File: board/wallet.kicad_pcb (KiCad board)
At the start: 4 copper layers, 48 x 85 mm, 136 parts, among them J1 TYPE-C-31-M-12, U1 BQ25185DLHR, U10 SN74LVC1T45DBVR, U11 E73-2G4M08S1C, U12 ME6211C28M5G-N, U13 TPS60230RGTR, U14 TLV75801PDBVR, U15 MAX17048G+T10, U2 TPS63802DLAR, U3 XC6206P332MR-G, U4 STM32U585VIT6Q, U5 SE050E2HQ1/Z01Z3Z, U6 TS3USB221ARSER, U7 SN74LVC1G02DBVR(UMW), U8 TPS22917DBVR, U9 SN74LVC1T45DBVR, Y1 Q13FC13500049

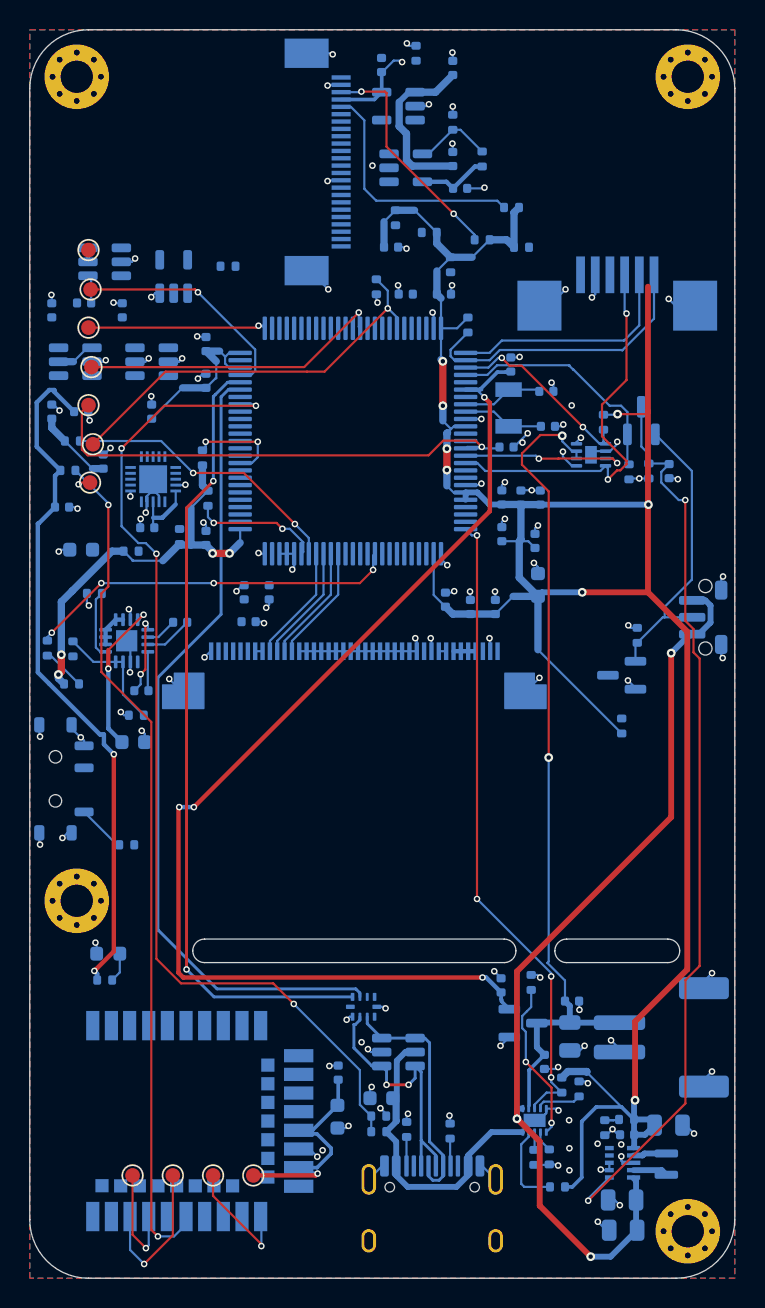
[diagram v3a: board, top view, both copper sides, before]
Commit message: Simplify the netlist (-28 parts), rip my auto-routing, camera pins ordered for J_CAM
Owner review: the pre-route was sloppy and the board too dense. This keeps all
of the owner's copper (minus what sat on removed parts or vanished nets) and
removes every track and via my partial router added.

Removed / merged (research in the commit's PR notes; each change checked
against the part's datasheet):
- radio UART isolation: two SN74LVC1T45 + 4 caps + 3 pull-ups -> one TI
  TXU0202 (fixed A1->B1Y, B2->A2Y; Hi-Z below 100 mV on either supply,
  Ioff; SCES942A 9.3.4) + 2 caps; OE on RADIO_3V3, so the hardware airgap
  guarantee is unchanged
- RTC backup chain (XC6206, 2 caps) and the 32 kHz crystal + 2 caps: VBAT on
  V3V3 (keeps its 100 nF); USB on HSI48+CRS, timeouts on LSI
- VREF+ shares VDDA's caps; VDD11's optional 100 nF caps
- camera: PWDN tied low at J_CAM, no RESET/PWDN pull-ups; DVDD on a fixed
  TLV70313 (no divider); one input cap for both camera LDOs
- R_CTPRST, R_BTNN (PA0 internal pull-up), R_ALRT + GAUGE_ALRT
- test pads SWO, BOOT0, RADIO_RESET
Camera pins: XCLK from TIM3_CH2 on PB5 and RST on PE0, so the north row is
in J_CAM's order (camera-bus trial route: 36 vias vs 40).

Tooling: syncBoard no longer segfaults swapping a back-side land (add before
Flip); checkMcuAf also catches nets dropped from the table; optimizePins can
put a timer clock on any TIMx_CHy pin; partialRoute: back-copper block wiring,
power may use In2, no necking, GND fanout vias keep 0.25 mm from pads, only
caps and ICs get their own GND via, long block links left with their bus.

Co-Authored-By: Claude Opus 5.5 <noreply@anthropic.com>
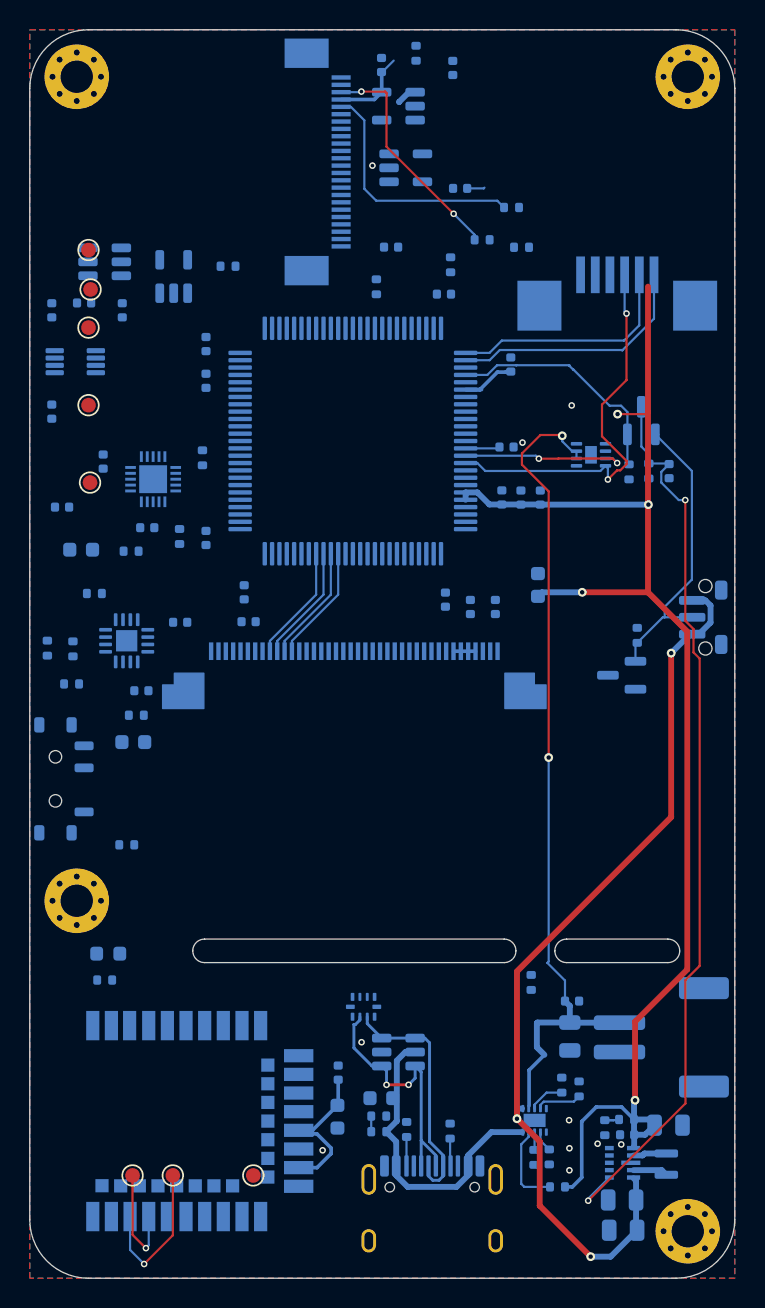
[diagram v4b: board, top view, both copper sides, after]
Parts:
- removed C_DVIN, C_RTC, C_RTCIN, C_VREF1: 1uF, Capacitor_SMD:C_0402_1005Metric
- removed C_LSE1, C_LSE2: 8pF, Capacitor_SMD:C_0402_1005Metric
- removed C_U10A, C_U10B, C_VDD11C, C_VDD11D, C_VREF2: 100nF, Capacitor_SMD:C_0402_1005Metric
- removed R_ALRT, R_BTNN, R_CRST, R_DV2, R_PWDN, R_RMTX, R_RRXPU, R_RTXPU: 100k, Resistor_SMD:R_0402_1005Metric
- removed R_CTPRST: 10k, Resistor_SMD:R_0402_1005Metric
- removed R_DV1: 137k, Resistor_SMD:R_0402_1005Metric
- removed TP_BOOT0: TP_BOOT0, TestPoint:TestPoint_Pad_D1.0mm
- removed TP_RRESET: TP_RRESET, TestPoint:TestPoint_Pad_D1.0mm
- removed TP_SWO: TP_SWO, TestPoint:TestPoint_Pad_D1.0mm
- removed U10: SN74LVC1T45DBVR, Package_TO_SOT_SMD:SOT-23-6
- removed U3: XC6206P332MR-G, Package_TO_SOT_SMD:SOT-23
- removed Y1: Q13FC13500049, Crystal:Crystal_SMD_3215-2Pin_3.2x1.5mm
- U14: value TLV75801PDBVR -> TLV70313DBVR
- U9: value SN74LVC1T45DBVR -> TXU0202DCUR; footprint Package_TO_SOT_SMD:SOT-23-6 -> Package_SO:VSSOP-8_2.3x2mm_P0.5mm
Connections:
- C_VBAT pad 1: VBAT_RTC -> V3V3
- J_CAM pad 17: CAM_PWDN -> GND
- U11 pad 26: RADIO_RESET -> (no net)
- U14 pad 4: CAM_DVFB -> GND
- U15 pad 5: GAUGE_ALRT -> NC_GAUGE_ALRT
- U4 pad 3: GAUGE_ALRT -> (no net)
- U4 pad 6: VBAT_RTC -> V3V3
- U4 pad 62: CAM_PWDN -> (no net)
- U4 pad 67: CAM_XCLK -> (no net)
- U4 pad 8: LSE_IN -> (no net)
- U4 pad 88: CAM_RST -> (no net)
- U4 pad 89: SWO -> (no net)
- U4 pad 9: LSE_OUT -> (no net)
- U4 pad 91: (no net) -> CAM_XCLK
- U4 pad 97: (no net) -> CAM_RST
- U9 pad 1: V3V3 -> RADIO_TX
- U9 pad 3: RADIO_TXD_MCU -> V3V3
- U9 pad 4: RADIO_RX -> RADIO_RXD_MCU
- U9 pad 5: V3V3 -> RADIO_TXD_MCU
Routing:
- net V3V3: track 236.9 -> 102.7 mm, vias 12 -> 4
- net GND: track 118.8 -> 1.20 mm, vias 122 -> 10
- net VBAT_RTC: track 78.7 -> 0.00 mm, vias 4 -> 0
- net VBUS_SENSE: track 69.0 -> 1.06 mm, vias 4 -> 0
- net RADIO_TX: track 57.7 -> 0.00 mm, vias 2 -> 0
- net USB_DN_MCU: track 55.4 -> 0.00 mm
- net USB_DP_MCU: track 54.1 -> 0.00 mm, vias 2 -> 0
- net RADIO_3V3: track 64.1 -> 10.1 mm, vias 3 -> 0
- net CHG_STAT2: track 44.0 -> 2.71 mm, vias 4 -> 0
- net NRST: track 34.7 -> 2.34 mm, vias 1 -> 0
- net BOOT0: track 27.8 -> 0.00 mm, vias 1 -> 0
- net AIRGAP_SENSE: track 25.5 -> 0.00 mm, vias 4 -> 0
- net SWO: track 20.9 -> 0.00 mm, vias 1 -> 0
- net RADIO_TXD_MCU: track 19.4 -> 0.00 mm, vias 2 -> 0
- net SWDIO: track 15.5 -> 0.00 mm, vias 1 -> 0
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
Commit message: Placement for routing: camera fan-in cleared, radio translator at the radio, decaps at their pins
- J_CAM's pads are entered from the east, where the camera LDOs left 1.2 mm
  for 24 lines: the LDO cluster (now ME6211 + fixed TLV70313, shared input
  cap) moved east of a 3.1 mm "Camera fan-in" keep-out, BOOT0's pull-down out
  of the bus approach. Your camera SDA/SCL/AVDD tracks there are removed.
- J_CAM stays: moved 4.5 mm east (to take a stock 21 mm module flat) its body
  would sit over the MCU's north pin row and cost every north camera pin a via.
  checkFpc now holds the camera tail to a budget: stock modules bow 4.2-4.8 mm
  (a ~16.5 mm custom flex lies flat).
- TXU0202 moved to the strip between the TFT slot and the radio module, right
  over the module's north-edge pads; the radio UART moves to P0.31/P0.30
  (pads 9/10), so no radio line crosses under the module.
- "MCU west escape" keep-out (pins 52-67): the SE pull-up moved out of it.
- Decaps at their pins: VDD11 one per pin (49, 98), C_VBAT clear of the
  PWR_HOLD track that ran between its pads, the battery gauge's cap at the gauge.
- scripts/refreshKeepouts.py redraws the rule areas on a hand-worked board
  from newBoard.py (the camera flex and fan-in follow J_CAM).

DRC: no errors besides 13 starved GND thermals (fanouts come with routing)
and the owner's pre-existing 8.5 mm V3V3 F.Cu stub.

Co-Authored-By: Claude Opus 5.5 <noreply@anthropic.com>
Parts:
- moved U9 44.2 mm to (15.1, 65.1), turned to 0 degrees
- moved C_U9A 40.5 mm to (12.2, 65.1), turned to -90 degrees
- moved C_GAUGE 37.2 mm to (35.9, 28.9), turned to -90 degrees
- moved C_U9B 36.2 mm to (18.0, 65.1), turned to 90 degrees
- moved C_VDD11B 23.7 mm to (27.4, 18.3)
- moved R_CAMEN 7.61 mm to (32.2, 6.40), turned to 0 degrees
- moved R_BOOT0 7.60 mm to (31.2, 17.4), turned to 0 degrees
- moved C_DOVDD 6.21 mm to (28.1, 9.70), turned to 180 degrees
- moved R_CSCL 5.87 mm to (27.4, 14.4), turned to 90 degrees
- moved C_DVOUT 5.74 mm to (26.1, 6.00), turned to 90 degrees
- moved U12 4.07 mm to (28.8, 3.50)
- moved U14 3.94 mm to (28.8, 7.10), turned to 180 degrees
- moved R_SESDA 3.16 mm to (9.00, 27.6), turned to 0 degrees
- moved C_VDD11A 2.95 mm to (16.3, 37.7), turned to -90 degrees
- moved C_AVIN 2.82 mm to (31.6, 2.90), turned to -90 degrees
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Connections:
- U11 pad 10: (no net) -> RADIO_RX
- U11 pad 33: RADIO_TX -> (no net)
- U11 pad 35: RADIO_RX -> (no net)
- U11 pad 9: (no net) -> RADIO_TX
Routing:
- net CAM_SCL: track 16.7 -> 0.00 mm
- net CAM_SDA: track 15.6 -> 0.00 mm, vias 2 -> 0
- net V3V3: track 102.7 -> 97.1 mm
- net CAM_AVDD: track 5.50 -> 0.00 mm
- net GND: track 1.20 -> 0.00 mm, vias 10 -> 9

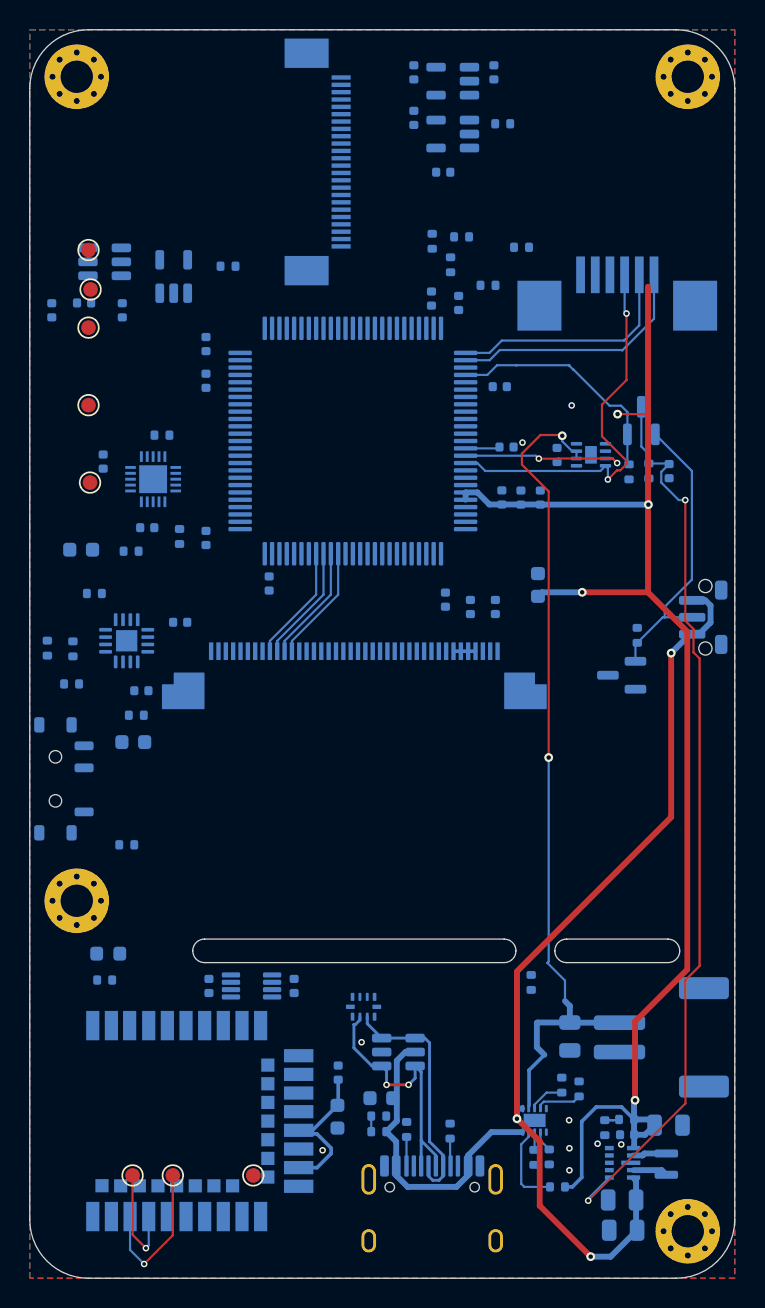
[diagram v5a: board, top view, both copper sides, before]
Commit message: Stack-up fixed (In2 solid GND, In1 the 3.3 V plane); blocks pre-routed cleanly
Stack-up: every part sits on B.Cu, whose return currents run in In2, but In2
was the "GND poured around power runs" layer and In1 the solid GND. Swapped:
In2 is solid GND (DRU: GND only), In1 is a V3V3 plane (DRU: V3V3, plus the
VDD11 core link). Every V3V3 pin and decap now drops a short via to In1, so no
3.3 V trunk runs on the outer layers.

Block wiring (scripts/partialRoute.py, on humanRouter's new keep-copper API
and knobs): back copper only; GND vias only for caps and ICs, 0.25 mm clear
of every pad, plus any pad the pour starves; no necking; test-pad, pull-up
and power links longer than 7/10 mm are left with their highway. Result: 144/145
block links + plane fanouts; new copper 202 mm B.Cu, 16 mm In1 (VDD11),
5 mm F.Cu (one radio test pad); the front is free for the highways.

Placement for this: the backlight pump turned 180 deg (cathodes/VOUT toward
J_TFT, flying caps west, input/output caps at VIN/VOUT, which the loop around
the chip showed); the SE 1.1 mm west with its input cap at VIN and its pull-ups
at their pins; BOOT0 tied to GND (bootloader via option bytes) so no pull-down
link crosses the camera pins, its via inside the pin ring.

Gauges on what is left for the hand route: KiCadRoutingTools routes all of it
(0 failed, 119 vias; before this pass 2-5 nets failed); humanRouter's full
finish routes all of it too (0 unconnected, 230 s).

Co-Authored-By: Claude Opus 5.5 <noreply@anthropic.com>
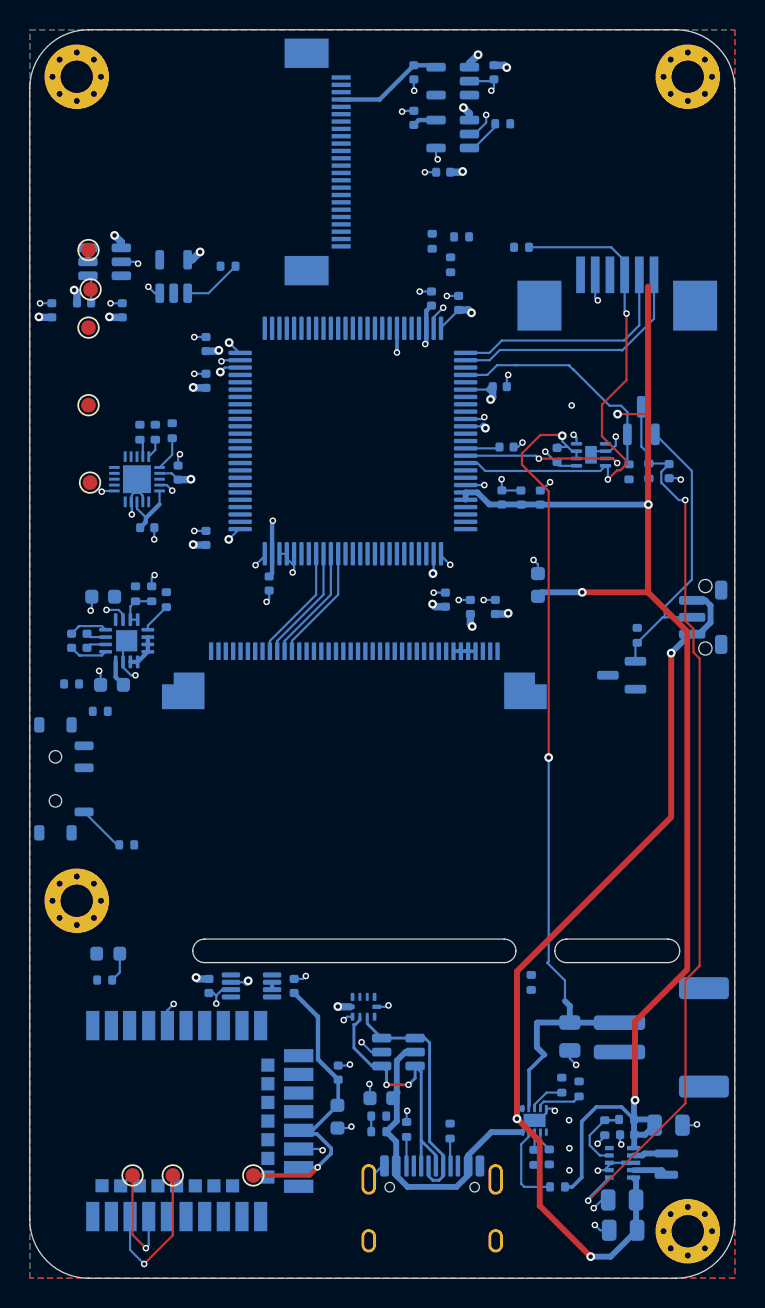
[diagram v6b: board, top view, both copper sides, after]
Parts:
- removed R_BOOT0: 10k, Resistor_SMD:R_0402_1005Metric
- moved R_BLPD 8.33 mm to (8.30, 38.4), turned to 90 degrees
- moved R_SESCL 8.27 mm to (8.55, 27.4), turned to 90 degrees
- moved R_SEENA 7.22 mm to (9.70, 27.3), turned to 90 degrees
- moved C_BLF1 6.47 mm to (3.90, 41.6), turned to 90 degrees
- moved C_BLF2 5.84 mm to (2.85, 41.6), turned to 90 degrees
- moved R_BLEN 5.68 mm to (7.20, 38.4), turned to -90 degrees
- moved R_AIRS 5.61 mm to (4.80, 46.4), turned to 0 degrees
- moved C_SEIN 5.15 mm to (10.1, 30.1)
- moved R_BLSET 4.92 mm to (9.30, 38.8), turned to 90 degrees
- moved C_BLOUT 4.16 mm to (5.60, 44.6), turned to 180 degrees
- moved C_BLIN 3.53 mm to (5.00, 38.6)
- moved R_SESDA 1.51 mm to (7.50, 27.4), turned to 90 degrees
- moved U5 1.10 mm to (7.30, 30.6)
- turned C_SEVCC to 0 degrees
- turned R_CSCL to -90 degrees
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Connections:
- U4 pad 94: BOOT0 -> GND
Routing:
- net GND: track 0.00 -> 85.7 mm, vias 9 -> 70
- net V3V3: track 97.1 -> 128.7 mm, vias 4 -> 30
- net VDD11: track 0.00 -> 23.0 mm, vias 0 -> 2
- net RADIO_3V3: track 10.1 -> 23.3 mm, vias 0 -> 1
- net I2C_SDA: track 26.9 -> 34.8 mm
- net CAM_AVDD: track 0.00 -> 7.48 mm
- net SE_VCC: track 0.00 -> 4.38 mm
- net RADIO_OFF: track 0.00 -> 4.02 mm
- net FB_3V3: track 1.58 -> 5.33 mm
- net AIR_THROW: track 0.00 -> 3.32 mm
- net BL_EN: track 0.00 -> 3.00 mm
- net BL_K: track 1.50 -> 4.28 mm
- net BL_C2N: track 0.00 -> 2.66 mm
- net BL_C2P: track 0.00 -> 2.63 mm
- net CAM_EN: track 0.00 -> 2.56 mm
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- added copper zone on In1.Cu, net V3V3
- removed copper zone on In1.Cu, net GND

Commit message: Plane vias for 3.3 V pull-ups and connector pins
The router's caps-and-ICs fanout policy deferred every plane pad of a resistor
or connector, which only works for GND (the outer pours pick those up). The
3.3 V pins of pull-ups, TP_3V3 and the J_TFT / J_CTP / J_CAM supply pins now get
their via to the In1 plane: 18 links, 13 vias; unconnected 79 -> 61, all of them
the buses left for the hand route.

Co-Authored-By: Claude Opus 5.5 <noreply@anthropic.com>
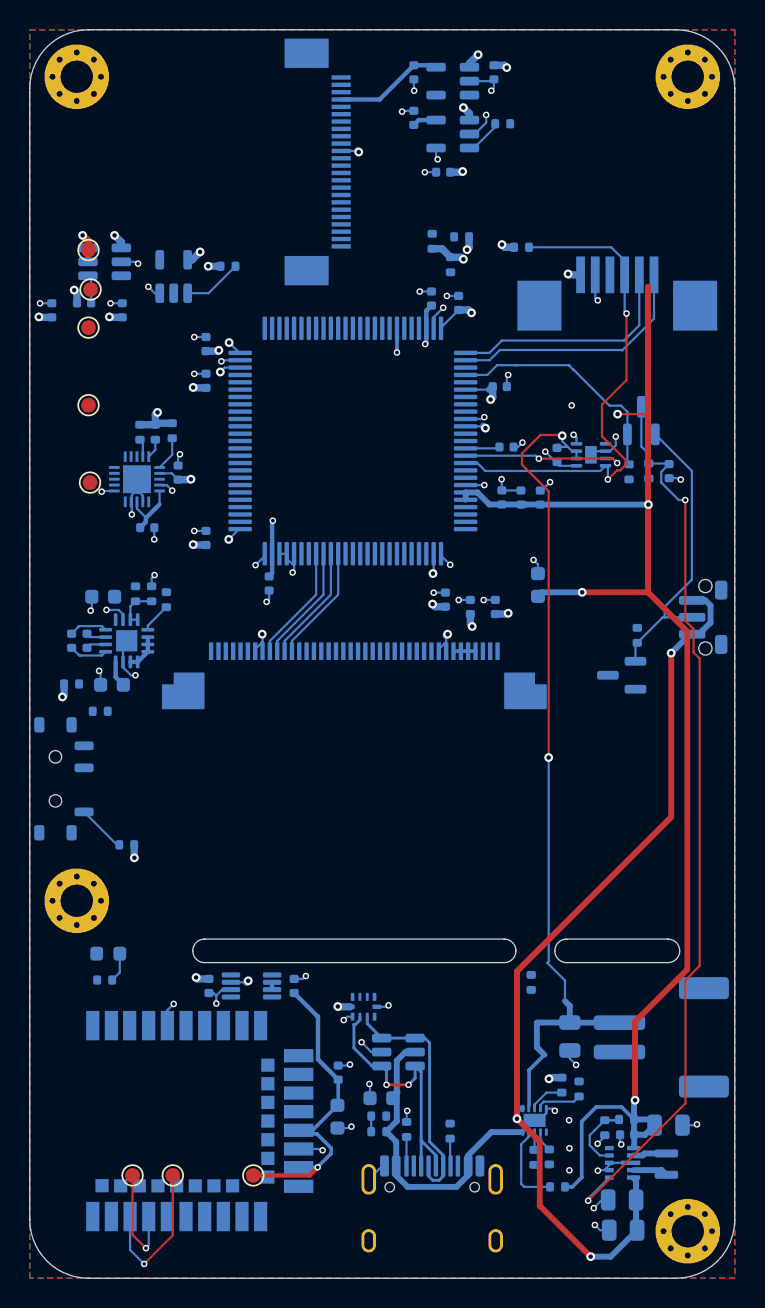
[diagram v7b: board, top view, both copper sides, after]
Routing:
- net V3V3: track 128.7 -> 147.0 mm, vias 30 -> 43
